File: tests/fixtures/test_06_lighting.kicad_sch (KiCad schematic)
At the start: 2 parts

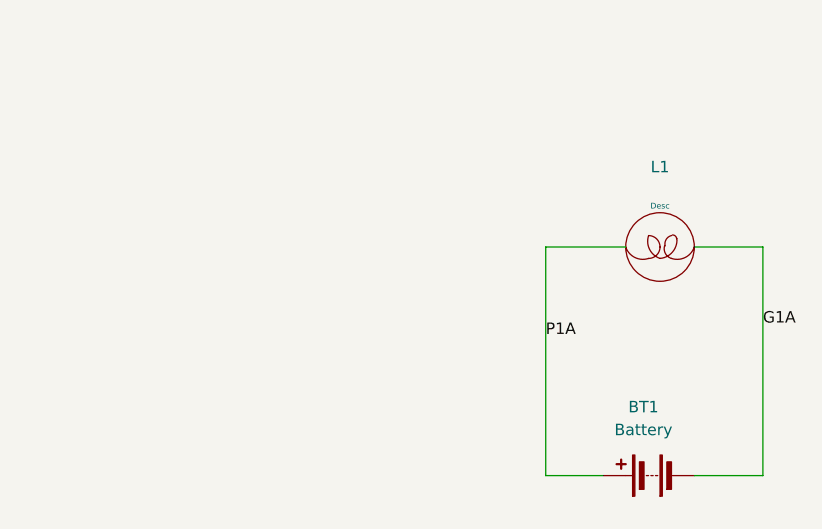
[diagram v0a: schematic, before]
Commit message: Migrate test fixtures from Footprint to LocLoad custom field
Move component location and electrical load encoding from overloaded
Footprint field to new custom LocLoad field. Remove leading pipe
character from encoding format.

Changes:
- Clear Footprint field values (restore to empty string)
- Add LocLoad custom property with format: (FS,WL,BL){S|L|R|G}<value>
- Remove leading | character from encoding format
- Add test_06 fixture files for new test cases

All fixtures now use LocLoad field as single source of component data.

🤖 Generated with [Claude Code](https://claude.com/claude-code)

Co-Authored-By: Claude <noreply@anthropic.com>
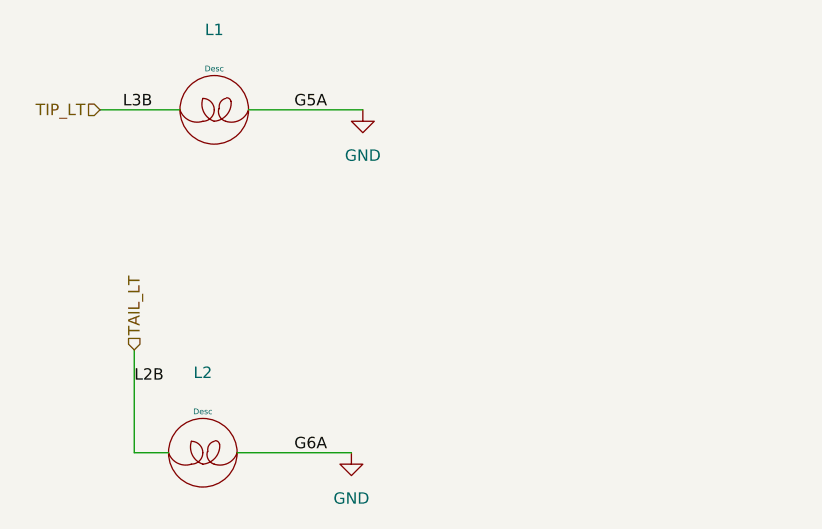
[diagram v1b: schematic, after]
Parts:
- removed BT1: Battery, symbol Device:Battery
- added L2: ~, symbol AeroElectricConnectionSymbols:Lamp
- L1: CInfo (none) -> |(0,0,100)L2.4; LocLoad (20,0,0)L1.5 -> (none)
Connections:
- net G1A renamed GND
- net GND: now also L2.2 (Out)
- net P1A renamed TIP_LT
- new net TAIL_LT: L2.1 (In)
